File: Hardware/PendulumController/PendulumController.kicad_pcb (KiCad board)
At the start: 2 copper layers, 157 x 47 mm, 60 parts, among them J101 MOTOR, J102 ENCODER, J201 ICSP, J302 19V Input, J401 USB_B_Micro, J402 PROG, SW201 RESET, SW202 START_SW, SW203 STOP/MODE_SW, U201 ATmega328P, U301 NCV1117ST50T3G, U401 FT232RL, Y201 16mHz

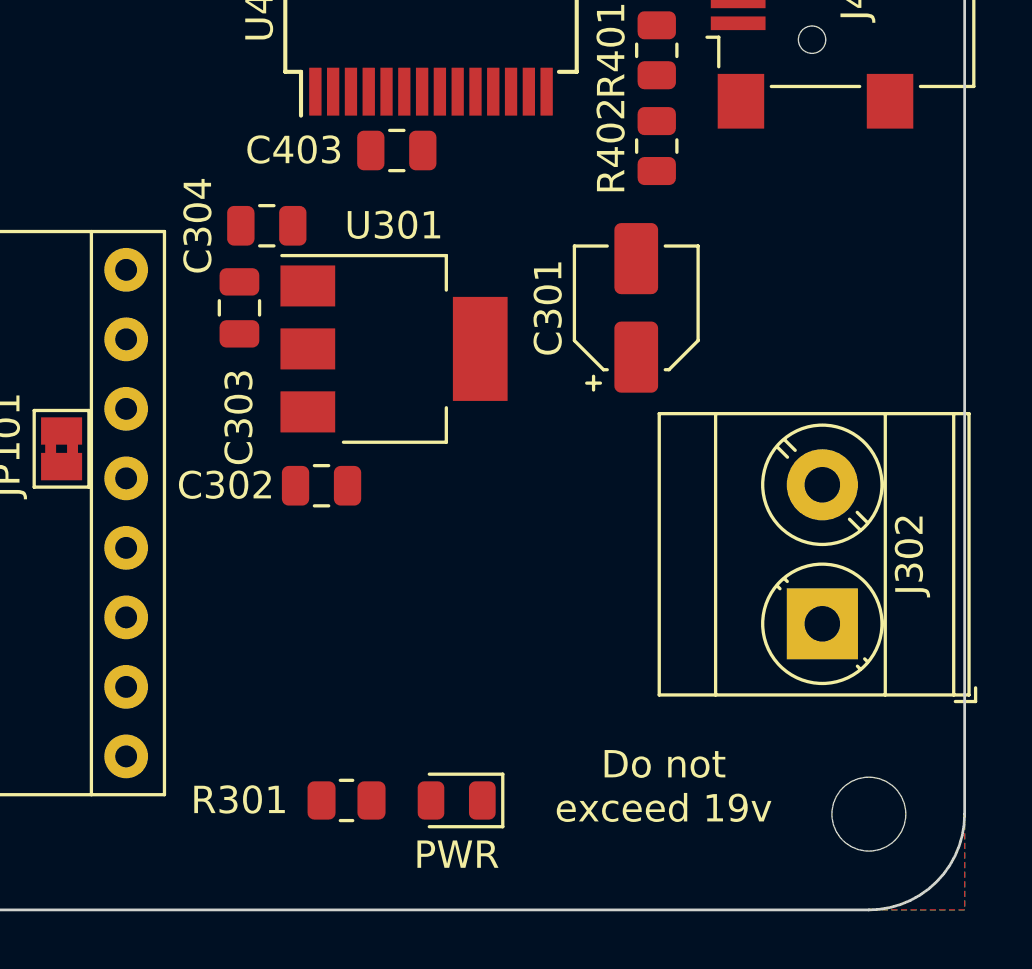
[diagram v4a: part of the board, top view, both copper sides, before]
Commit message: Finalize input location
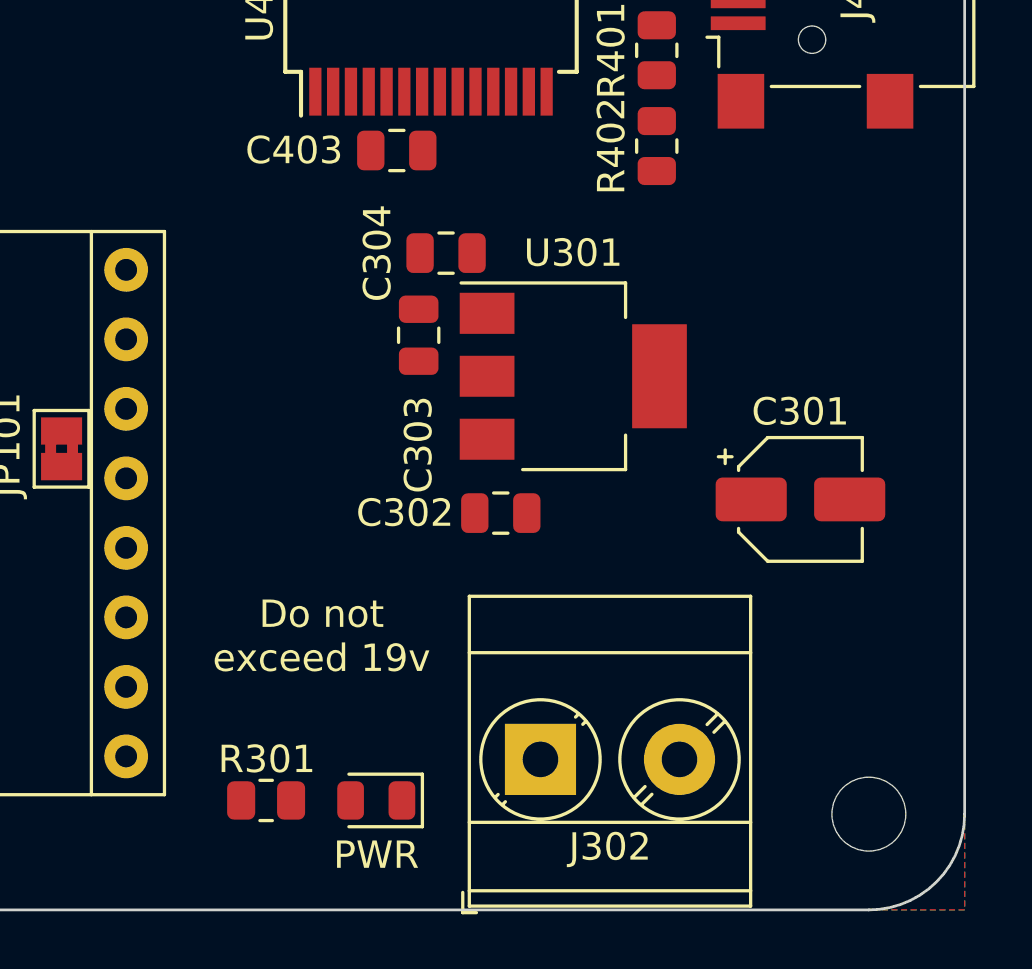
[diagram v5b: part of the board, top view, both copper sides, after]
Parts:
- moved J302 11.4 mm to (208.0, 108.0), turned to 0 degrees
- moved C301 9.22 mm to (217.5, 98.5), turned to 0 degrees
- moved C302 6.63 mm to (206.6, 99.0)
- moved C303 6.63 mm to (203.6, 92.5)
- moved C304 6.63 mm to (204.6, 89.5)
- moved U301 6.63 mm to (209.2, 94.0)
- moved D301 2.94 mm to (202.0, 109.5)
- moved R301 2.94 mm to (198.0, 109.5)
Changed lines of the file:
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@@
   )
   (footprint "Resistor_SMD:R_0805_2012Metric" (layer "F.Cu")
-    (at 200.9125 109.5)
+    (at 197.975 109.5)
     (descr "Resistor SMD 0805 (2012 Metric), square (rectangular) end terminal, IPC_7351 nominal, (Body size source: IPC-SM-782 page 72, https://www.pcb-3d.com/wordpress/wp-content/uploads/ipc-sm-782a_amendment_1_and_2.pdf), generated with kicad-footprint-generator")
     (tags "resistor")
@@
     (property "Sheetname" "Power")
     (attr smd)
-    (fp_text reference "R301" (at -3.9125 0) (layer "F.SilkS")
+    (fp_text reference "R301" (at 0.025 -1.5) (layer "F.SilkS")
       (effects (font (size 1 1) (thickness 0.15)))
     )
@@
   )
   (footprint "Capacitor_SMD:C_0805_2012Metric" (layer "F.Cu")
-    (at 200 98)
+    (at 206.55 99)
     (descr "Capacitor SMD 0805 (2012 Metric), square (rectangular) end terminal, IPC_7351 nominal, (Body size source: IPC-SM-782 page 76, https://www.pcb-3d.com/wordpress/wp-content/uploads/ipc-sm-782a_amendment_1_and_2.pdf, https://docs.google.com/spreadsheets/d/1BsfQQcO9C6DZCsRaXUlFlo91Tg2WpOkGARC1WS5S8t0/edit?usp=sharing), generated with kicad-footprint-generator")
     (tags "capacitor")
@@
   )
   (footprint "LED_SMD:LED_0805_2012Metric" (layer "F.Cu")
-    (at 204.9375 109.5 180)
+    (at 202 109.5 180)
     (descr "LED SMD 0805 (2012 Metric), square (rectangular) end terminal, IPC_7351 nominal, (Body size source: https://docs.google.com/spreadsheets/d/1BsfQQcO9C6DZCsRaXUlFlo91Tg2WpOkGARC1WS5S8t0/edit?usp=sharing), generated with kicad-footprint-generator")
     (tags "LED")
@@
   )
   (footprint "Package_TO_SOT_SMD:SOT-223" (layer "F.Cu")
-    (at 202.65 93)
+    (at 209.2 94)
     (descr "module CMS SOT223 4 pins")
     (tags "CMS SOT")
@@
   )
   (footprint "Capacitor_SMD:C_0805_2012Metric" (layer "F.Cu")
-    (at 198 88.5)
+    (at 204.55 89.5)
     (descr "Capacitor SMD 0805 (2012 Metric), square (rectangular) end terminal, IPC_7351 nominal, (Body size source: IPC-SM-782 page 76, https://www.pcb-3d.com/wordpress/wp-content/uploads/ipc-sm-782a_amendment_1_and_2.pdf, https://docs.google.com/spreadsheets/d/1BsfQQcO9C6DZCsRaXUlFlo91Tg2WpOkGARC1WS5S8t0/edit?usp=sharing), generated with kicad-footprint-generator")
     (tags "capacitor")
@@
   )
   (footprint "Capacitor_SMD:C_0805_2012Metric" (layer "F.Cu")
-    (at 197 91.5 90)
+    (at 203.55 92.5 90)
     (descr "Capacitor SMD 0805 (2012 Metric), square (rectangular) end terminal, IPC_7351 nominal, (Body size source: IPC-SM-782 page 76, https://www.pcb-3d.com/wordpress/wp-content/uploads/ipc-sm-782a_amendment_1_and_2.pdf, https://docs.google.com/spreadsheets/d/1BsfQQcO9C6DZCsRaXUlFlo91Tg2WpOkGARC1WS5S8t0/edit?usp=sharing), generated with kicad-footprint-generator")
     (tags "capacitor")
@@
   )
   (footprint "Capacitor_SMD:CP_Elec_4x3" (layer "F.Cu")
-    (at 211.5 91.5 90)
+    (at 217.5 98.5)
     (descr "SMD capacitor, aluminum electrolytic, Nichicon, 4.0x3mm")
     (tags "capacitor electrolytic")
@@
     (property "Sheetname" "Power")
     (attr smd)
-    (fp_text reference "C301" (at 0 -3.2 90) (layer "F.SilkS")
+    (fp_text reference "C301" (at 0 -3.2) (layer "F.SilkS")
       (effects (font (size 1 1) (thickness 0.15)))
     )
-    (fp_text value "10uf" (at 0 3.2 90) (layer "F.Fab")
+    (fp_text value "10uf" (at 0 3.2) (layer "F.Fab")
       (effects (font (size 1 1) (thickness 0.15)))
     )
-    (fp_text user "${REFERENCE}" (at 0 0 90) (layer "F.Fab")
+    (fp_text user "${REFERENCE}" (at 0 0) (layer "F.Fab")
       (effects (font (size 0.8 0.8) (thickness 0.12)))
     )
@@
     (fp_line (start -1.374773 -1.2) (end -1.374773 -0.8) (layer "F.Fab") (width 0.1))
     (fp_circle (center 0 0) (end 2 0) (layer "F.Fab") (width 0.1) (fill none))
-    (pad "1" smd roundrect (at -1.8 0 90) (size 2.6 1.6) (layers "F.Cu" "F.Paste" "F.Mask") (roundrect_rratio 0.15625)
+    (pad "1" smd roundrect (at -1.8 0) (size 2.6 1.6) (layers "F.Cu" "F.Paste" "F.Mask") (roundrect_rratio 0.15625)
       (net 29 "+19V") (pintype "passive"))
-    (pad "2" smd roundrect (at 1.8 0 90) (size 2.6 1.6) (layers "F.Cu" "F.Paste" "F.Mask") (roundrect_rratio 0.15625)
+    (pad "2" smd roundrect (at 1.8 0) (size 2.6 1.6) (layers "F.Cu" "F.Paste" "F.Mask") (roundrect_rratio 0.15625)
       (net 1 "GND") (pintype "passive"))
     (model "${KICAD6_3DMODEL_DIR}/Capacitor_SMD.3dshapes/CP_Elec_4x3.wrl"
@@
   )
   (footprint "TerminalBlock_Phoenix:TerminalBlock_Phoenix_MKDS-3-2-5.08_1x02_P5.08mm_Horizontal" (layer "F.Cu")
-    (at 218.3 103.045 90)
+    (at 208 108)
     (descr "Terminal Block Phoenix MKDS-3-2-5.08, 2 pins, pitch 5.08mm, size 10.2x11.2mm^2, drill diamater 1.3mm, pad diameter 2.6mm, see http://www.farnell.com/datasheets/2138224.pdf, script-generated using https://github.com/pointhi/kicad-footprint-generator/scripts/TerminalBlock_Phoenix")
     (tags "THT Terminal Block Phoenix MKDS-3-2-5.08 pitch 5.08mm size 10.2x11.2mm^2 drill 1.3mm pad 2.6mm")
@@
     (property "Sheetname" "Power")
     (attr through_hole)
-    (fp_text reference "J302" (at 2.545 3.2 270) (layer "F.SilkS")
+    (fp_text reference "J302" (at 2.545 3.2) (layer "F.SilkS")
       (effects (font (size 1 1) (thickness 0.15)))
     )
-    (fp_text value "19V Input" (at 2.54 6.36 90) (layer "F.Fab")
+    (fp_text value "19V Input" (at 2.54 6.36) (layer "F.Fab")
       (effects (font (size 1 1) (thickness 0.15)))
     )
-    (fp_text user "${REFERENCE}" (at 2.54 3.1 90) (layer "F.Fab")
+    (fp_text user "${REFERENCE}" (at 2.54 3.1) (layer "F.Fab")
       (effects (font (size 1 1) (thickness 0.15)))
     )
@@
     (fp_circle (center 0 0) (end 2 0) (layer "F.Fab") (width 0.1) (fill none))
     (fp_circle (center 5.08 0) (end 7.08 0) (layer "F.Fab") (width 0.1) (fill none))
-    (pad "1" thru_hole rect (at 0 0 90) (size 2.6 2.6) (drill 1.3) (layers *.Cu *.Mask)
+    (pad "1" thru_hole rect (at 0 0) (size 2.6 2.6) (drill 1.3) (layers *.Cu *.Mask)
       (net 1 "GND") (pinfunction "Pin_1") (pintype "passive"))
-    (pad "2" thru_hole circle (at 5.08 0 90) (size 2.6 2.6) (drill 1.3) (layers *.Cu *.Mask)
+    (pad "2" thru_hole circle (at 5.08 0) (size 2.6 2.6) (drill 1.3) (layers *.Cu *.Mask)
       (net 29 "+19V") (pinfunction "Pin_2") (pintype "passive"))
     (model "${KICAD6_3DMODEL_DIR}/TerminalBlock_Phoenix.3dshapes/TerminalBlock_Phoenix_MKDS-3-2-5.08_1x02_P5.08mm_Horizontal.wrl"
@@
   (gr_line (start 223.5 110) (end 223.5 70) (layer "Edge.Cuts") (width 0.1))
   (gr_rect (start 55 55) (end 235 135) (layer "F.Fab") (width 0.1) (fill none))
-  (gr_text "Do not\nexceed 19v" (at 212.5 109) (layer "F.SilkS")
+  (gr_text "Do not\nexceed 19v" (at 200 103.5) (layer "F.SilkS")
     (effects (font (size 1 1) (thickness 0.15)))
   )
